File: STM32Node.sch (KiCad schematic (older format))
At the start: 7 parts, among them J1 Conn_01x20, J2 Conn_01x18, J3 Conn_Coaxial, J4 Conn_01x03, U1 stm32f103c8t6-module-china, U2 RFM95W-868S2

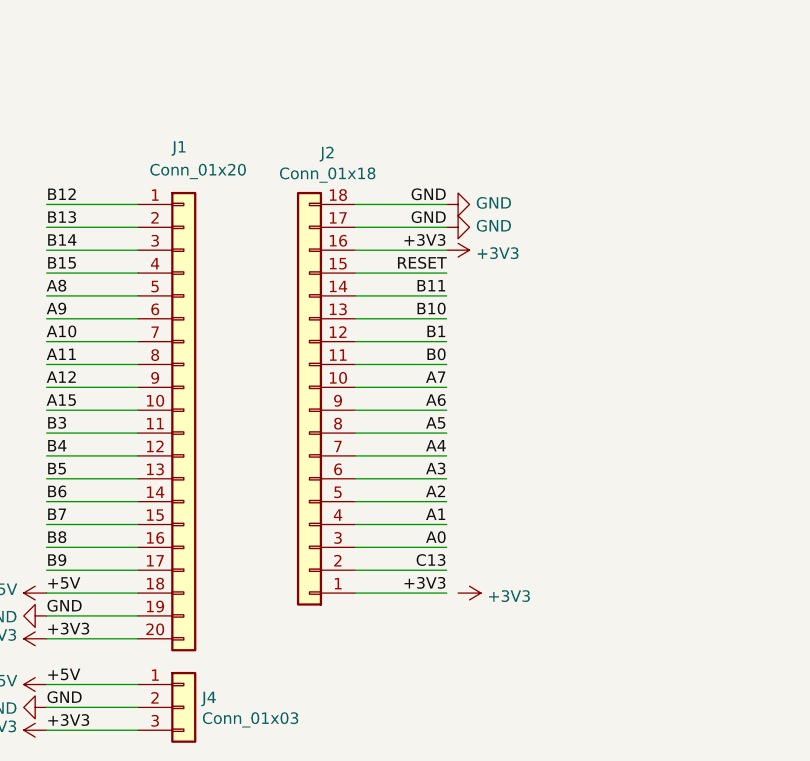
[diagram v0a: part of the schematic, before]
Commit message: resize board, that it fits into case
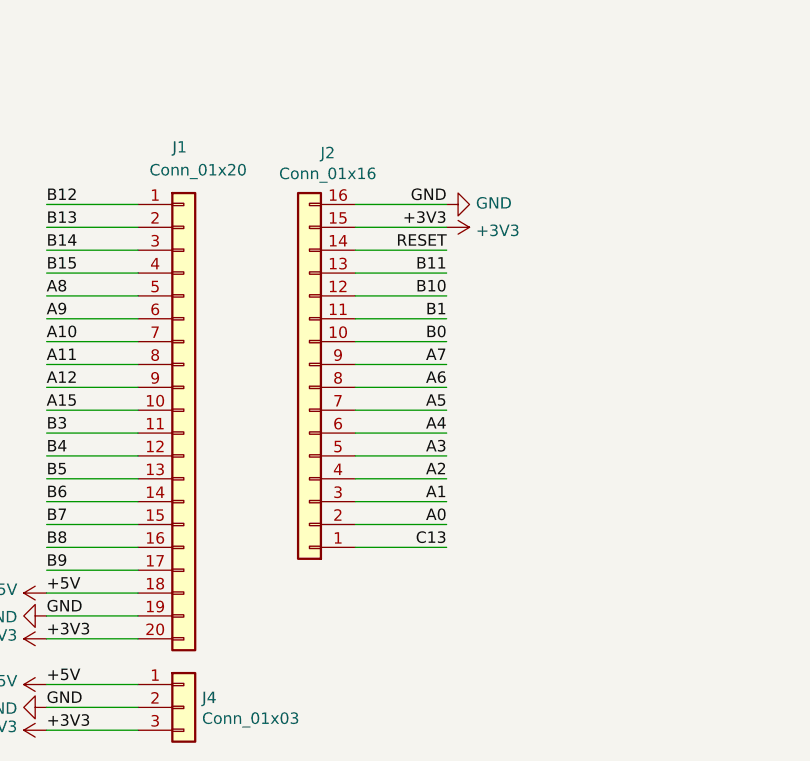
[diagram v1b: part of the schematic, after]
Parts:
- removed J2: Conn_01x18, Connector_PinSocket_2.54mm:PinSocket_1x18_P2.54mm_Vertical, symbol Connector_Generic:Conn_01x18
- added J2: Conn_01x16, Connector_PinSocket_2.54mm:PinSocket_1x16_P2.54mm_Vertical, symbol Connector_Generic:Conn_01x16
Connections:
- net +3V3: now also J2.15 (Pin_15)
- net A0: now also J2.2 (Pin_2)
- net A1: now also J2.3 (Pin_3)
- net A2: now also J2.4 (Pin_4)
- net A3: now also J2.5 (Pin_5)
- net A4: now also J2.6 (Pin_6)
- net A5: now also J2.7 (Pin_7)
- net A6: now also J2.8 (Pin_8)
- net A7: now also J2.9 (Pin_9)
- net B0: now also J2.10 (Pin_10)
- net B1: now also J2.11 (Pin_11)
- net B10: now also J2.12 (Pin_12)
- net B11: now also J2.13 (Pin_13)
- net C13: now also J2.1 (Pin_1)
- net GND: now also J2.16 (Pin_16)
- net RESET: now also J2.14 (Pin_14)
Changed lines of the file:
@@
 B7
 Wire Wire Line
-	3100 5150 2700 5150
-Wire Wire Line
-	2700 5250 3100 5250
-Wire Wire Line
-	3100 5350 2700 5350
-Wire Wire Line
-	2700 5450 3100 5450
-Wire Wire Line
-	3100 5550 2700 5550
-Wire Wire Line
-	2700 5650 3100 5650
-Wire Wire Line
-	3100 5750 2700 5750
-Wire Wire Line
-	2700 5850 3100 5850
-Wire Wire Line
-	3100 5950 2700 5950
-Wire Wire Line
-	2700 6050 3100 6050
-Wire Wire Line
-	3100 6150 2700 6150
-Wire Wire Line
-	2700 6250 3100 6250
-Wire Wire Line
-	3100 6350 2700 6350
-Wire Wire Line
-	2700 6450 3100 6450
-Wire Wire Line
-	3100 6550 2700 6550
-Wire Wire Line
-	2700 6650 3100 6650
-Wire Wire Line
-	3100 6750 2700 6750
-Wire Wire Line
-	2700 6850 3100 6850
+	2700 5150 3100 5150
+Wire Wire Line
+	3100 5250 2700 5250
+Wire Wire Line
+	2700 5350 3100 5350
+Wire Wire Line
+	3100 5450 2700 5450
+Wire Wire Line
+	2700 5550 3100 5550
+Wire Wire Line
+	3100 5650 2700 5650
+Wire Wire Line
+	2700 5750 3100 5750
+Wire Wire Line
+	3100 5850 2700 5850
+Wire Wire Line
+	2700 5950 3100 5950
+Wire Wire Line
+	3100 6050 2700 6050
+Wire Wire Line
+	2700 6150 3100 6150
+Wire Wire Line
+	3100 6250 2700 6250
+Wire Wire Line
+	2700 6350 3100 6350
+Wire Wire Line
+	3100 6450 2700 6450
+Wire Wire Line
+	2700 6550 3100 6550
+Wire Wire Line
+	3100 6650 2700 6650
 Text Label 3100 5150 2    50   ~ 0
 GND
 Text Label 3100 5250 2    50   ~ 0
-GND
++3V3
 Text Label 3100 5350 2    50   ~ 0
-+3V3
+RESET
 Text Label 3100 5450 2    50   ~ 0
-RESET
+B11
 Text Label 3100 5550 2    50   ~ 0
-B11
+B10
 Text Label 3100 5650 2    50   ~ 0
-B10
+B1
 Text Label 3100 5750 2    50   ~ 0
-B1
+B0
 Text Label 3100 5850 2    50   ~ 0
-B0
+A7
 Text Label 3100 5950 2    50   ~ 0
-A7
+A6
 Text Label 3100 6050 2    50   ~ 0
-A6
+A5
 Text Label 3100 6150 2    50   ~ 0
-A5
+A4
 Text Label 3100 6250 2    50   ~ 0
-A4
+A3
 Text Label 3100 6350 2    50   ~ 0
-A3
+A2
 Text Label 3100 6450 2    50   ~ 0
-A2
+A1
 Text Label 3100 6550 2    50   ~ 0
-A1
+A0
 Text Label 3100 6650 2    50   ~ 0
-A0
-Text Label 3100 6750 2    50   ~ 0
 C13
-Text Label 3100 6850 2    50   ~ 0
-+3V3
-$Comp
-L power:+3V3 #PWR0113
-U 1 1 5BF65FFA
-P 3150 6850
-F 0 "#PWR0113" H 3150 6700 50  0001 C CNN
-F 1 "+3V3" V 3165 6978 50  0000 L CNN
-F 2 "" H 3150 6850 50  0001 C CNN
-F 3 "" H 3150 6850 50  0001 C CNN
-	1    3150 6850
-	0    1    1    0
-$EndComp
 $Comp
 L power:+3V3 #PWR0114
 U 1 1 5BF66000
-P 3100 5350
-F 0 "#PWR0114" H 3100 5200 50  0001 C CNN
-F 1 "+3V3" V 3115 5478 50  0000 L CNN
-F 2 "" H 3100 5350 50  0001 C CNN
-F 3 "" H 3100 5350 50  0001 C CNN
-	1    3100 5350
+P 3100 5250
+F 0 "#PWR0114" H 3100 5100 50  0001 C CNN
+F 1 "+3V3" V 3115 5378 50  0000 L CNN
+F 2 "" H 3100 5250 50  0001 C CNN
+F 3 "" H 3100 5250 50  0001 C CNN
+	1    3100 5250
 	0    1    1    0
 $EndComp
 $Comp
-L power:GND #PWR0115
-U 1 1 5BF66006
+L power:GND #PWR0116
+U 1 1 5BF6600C
 P 3100 5150
-F 0 "#PWR0115" H 3100 4900 50  0001 C CNN
+F 0 "#PWR0116" H 3100 4900 50  0001 C CNN
 F 1 "GND" V 3105 5022 50  0000 R CNN
 F 2 "" H 3100 5150 50  0001 C CNN
 F 3 "" H 3100 5150 50  0001 C CNN
 	1    3100 5150
-	0    -1   -1   0
-$EndComp
-$Comp
-L power:GND #PWR0116
-U 1 1 5BF6600C
-P 3100 5250
-F 0 "#PWR0116" H 3100 5000 50  0001 C CNN
-F 1 "GND" V 3105 5122 50  0000 R CNN
-F 2 "" H 3100 5250 50  0001 C CNN
-F 3 "" H 3100 5250 50  0001 C CNN
-	1    3100 5250
 	0    -1   -1   0
 $EndComp
@@
 $EndComp
 $Comp
-L Connector_Generic:Conn_01x18 J2
-U 1 1 5BFECD70
-P 2500 6050
-F 0 "J2" H 2420 4925 50  0000 C CNN
-F 1 "Conn_01x18" H 2420 5016 50  0000 C CNN
-F 2 "Connector_PinSocket_2.54mm:PinSocket_1x18_P2.54mm_Vertical" H 2500 6050 50  0001 C CNN
-F 3 "~" H 2500 6050 50  0001 C CNN
-	1    2500 6050
-	-1   0    0    1
-$EndComp
-$Comp
 L Connector_Generic:Conn_01x03 J4
 U 1 1 5BFF4F29
@@
 Text Label 8900 2350 2    50   ~ 0
 B5
+$Comp
+L Connector_Generic:Conn_01x16 J2
+U 1 1 5CA11824
+P 2500 5950
+F 0 "J2" H 2420 4925 50  0000 C CNN
+F 1 "Conn_01x16" H 2420 5016 50  0000 C CNN
+F 2 "Connector_PinSocket_2.54mm:PinSocket_1x16_P2.54mm_Vertical" H 2500 5950 50  0001 C CNN
+F 3 "~" H 2500 5950 50  0001 C CNN
+	1    2500 5950
+	-1   0    0    1
+$EndComp
 $EndSCHEMATC
